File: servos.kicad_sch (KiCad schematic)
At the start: 16 parts, among them J10 Conn_01x03_Male, J18 Conn_01x03_Male, J19 Conn_01x03_Male, J5 Conn_01x03_Male, J6 Conn_01x03_Male, J7 Conn_01x03_Male, J8 Conn_01x03_Male, J9 Conn_01x03_Male, Q6 DMN2011UTS

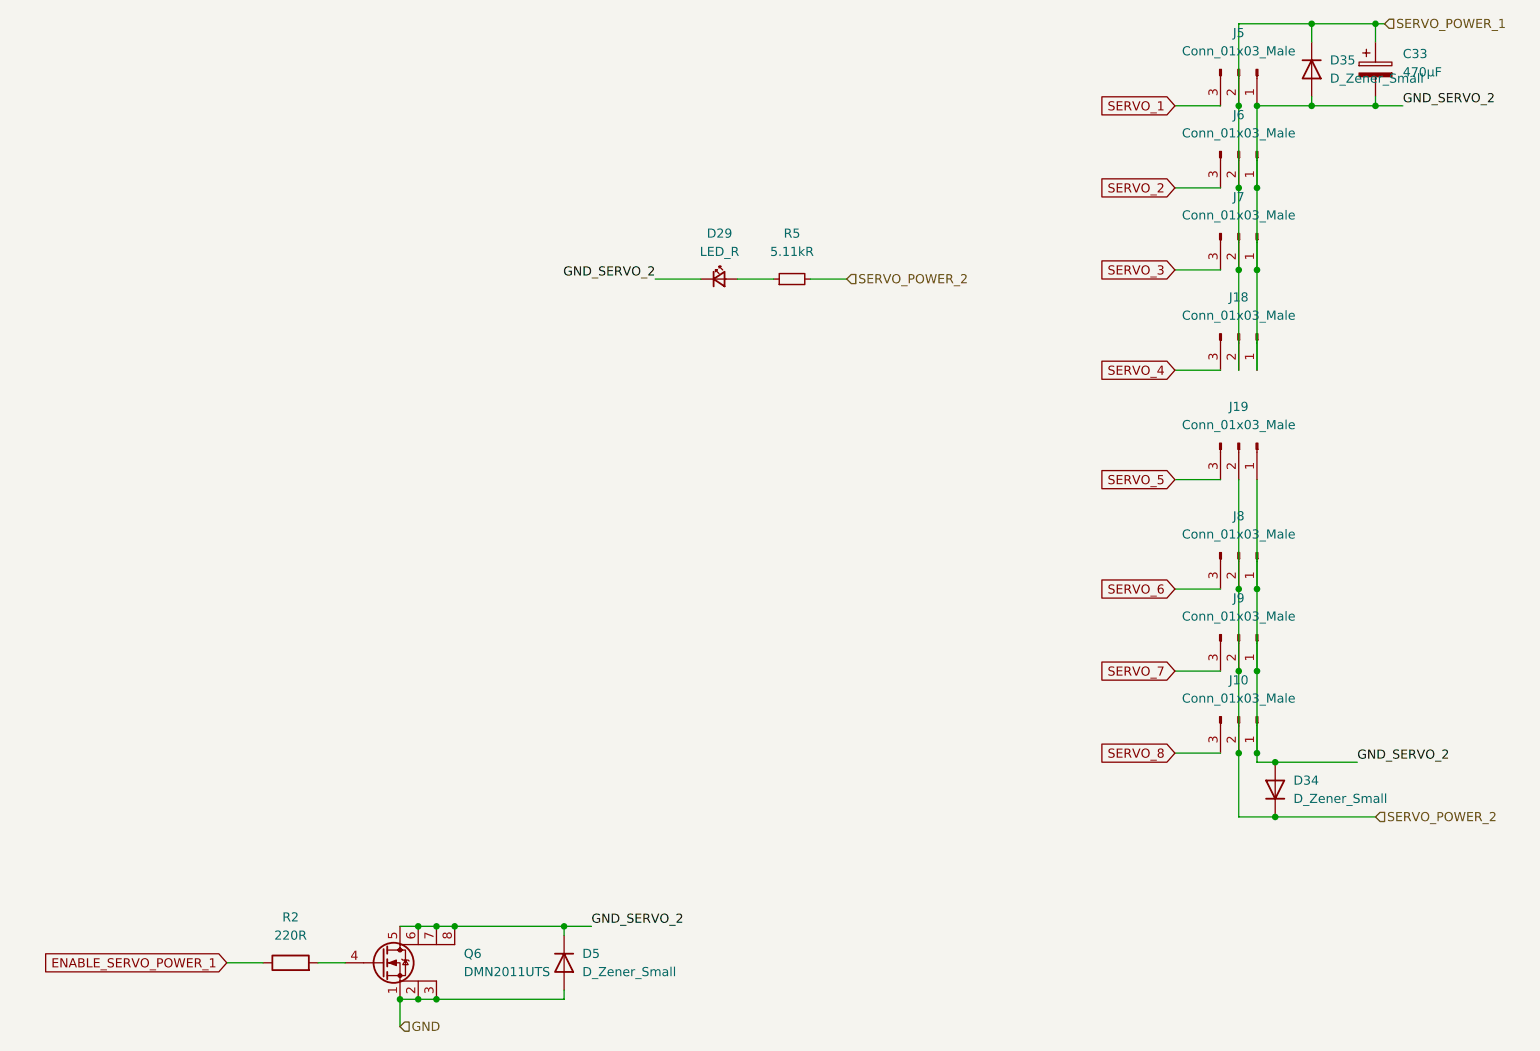
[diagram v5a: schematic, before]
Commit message: update BOM + add big capas (do not take DNP into account)
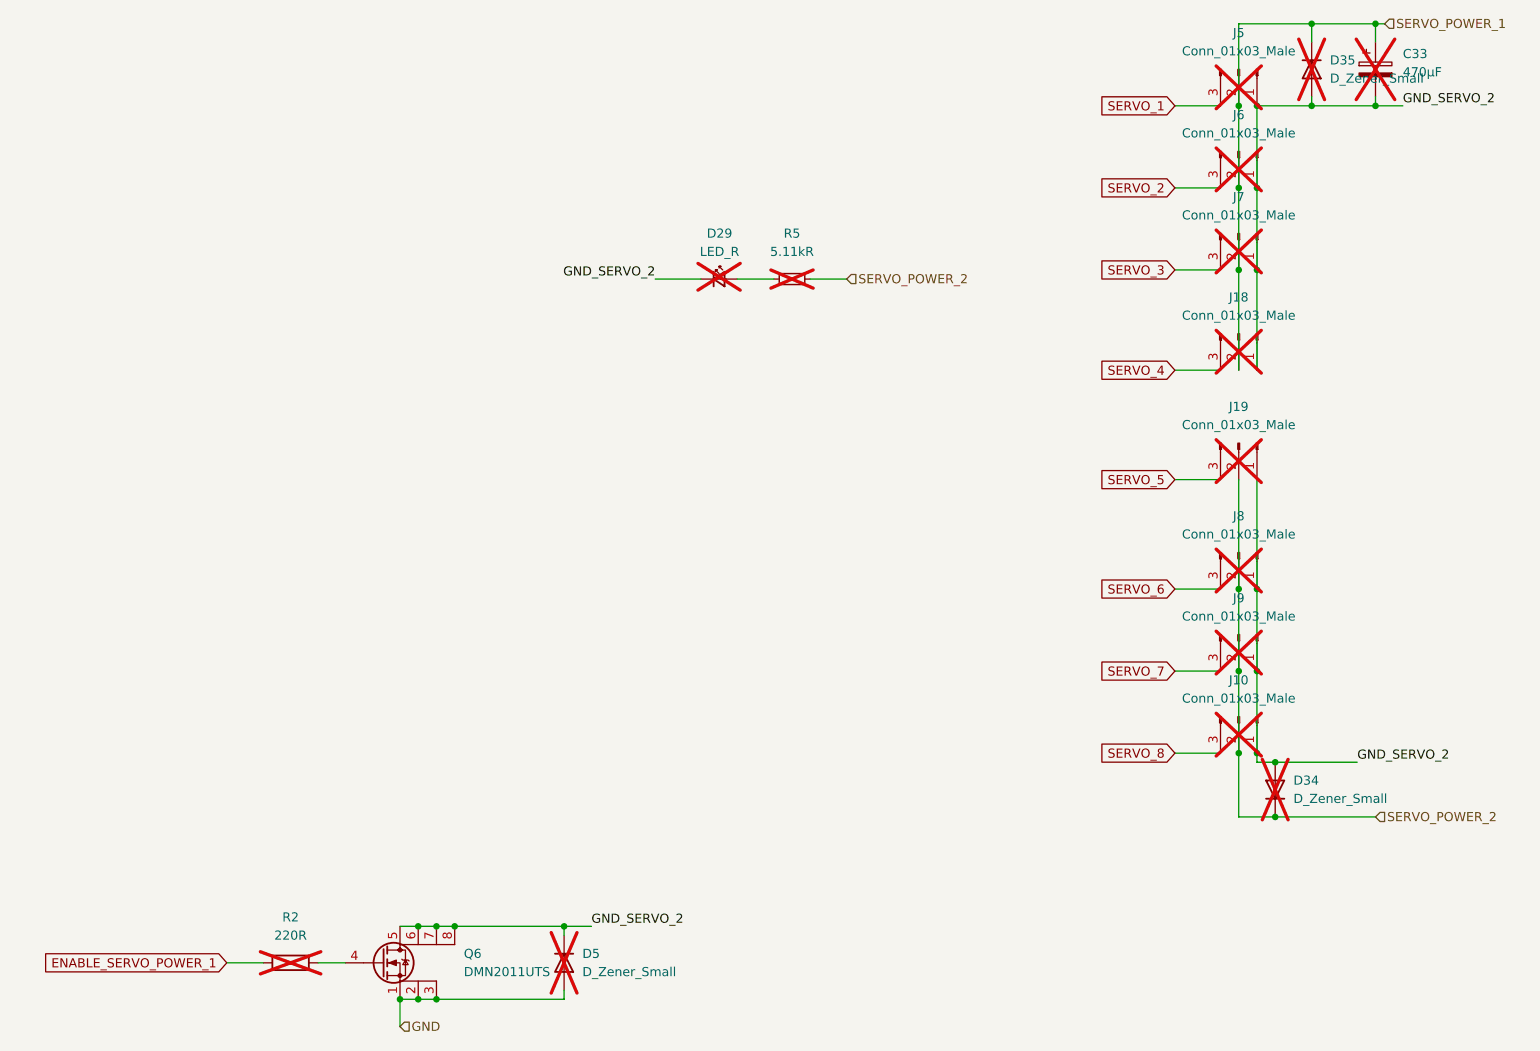
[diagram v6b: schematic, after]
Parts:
- C33, D29, D34, D35, D5, J10, J18, J19, J5, J6, J7, J8, J9, R2, R5: now not fitted
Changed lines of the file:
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@@
 		(in_bom yes)
 		(on_board yes)
-		(dnp no)
+		(dnp yes)
 		(fields_autoplaced yes)
 		(property "Reference" "D5"
@@
 		(in_bom yes)
 		(on_board yes)
-		(dnp no)
+		(dnp yes)
 		(fields_autoplaced yes)
 		(property "Reference" "J7"
@@
 		(in_bom yes)
 		(on_board yes)
-		(dnp no)
+		(dnp yes)
 		(property "Reference" "J19"
 			(at 210.82 99.06 90)
@@
 		(in_bom yes)
 		(on_board yes)
-		(dnp no)
+		(dnp yes)
 		(fields_autoplaced yes)
 		(property "Reference" "D29"
@@
 		(in_bom yes)
 		(on_board yes)
-		(dnp no)
+		(dnp yes)
 		(fields_autoplaced yes)
 		(property "Reference" "J5"
@@
 		(in_bom yes)
 		(on_board yes)
-		(dnp no)
+		(dnp yes)
 		(fields_autoplaced yes)
 		(property "Reference" "C33"
@@
 		(in_bom yes)
 		(on_board yes)
-		(dnp no)
+		(dnp yes)
 		(fields_autoplaced yes)
 		(property "Reference" "D34"
@@
 		(in_bom yes)
 		(on_board yes)
-		(dnp no)
+		(dnp yes)
 		(fields_autoplaced yes)
 		(property "Reference" "J6"
@@
 		(in_bom yes)
 		(on_board yes)
-		(dnp no)
+		(dnp yes)
 		(fields_autoplaced yes)
 		(property "Reference" "D35"
@@
 		(in_bom yes)
 		(on_board yes)
-		(dnp no)
+		(dnp yes)
 		(fields_autoplaced yes)
 		(property "Reference" "R5"
@@
 		(in_bom yes)
 		(on_board yes)
-		(dnp no)
+		(dnp yes)
 		(fields_autoplaced yes)
 		(property "Reference" "J10"
@@
 		(in_bom yes)
 		(on_board yes)
-		(dnp no)
+		(dnp yes)
 		(fields_autoplaced yes)
 		(property "Reference" "J18"
@@
 		(in_bom yes)
 		(on_board yes)
-		(dnp no)
+		(dnp yes)
 		(fields_autoplaced yes)
 		(property "Reference" "J9"
@@
 		(in_bom yes)
 		(on_board yes)
-		(dnp no)
+		(dnp yes)
 		(property "Reference" "J8"
 			(at 210.82 114.3 90)
@@
 		(in_bom yes)
 		(on_board yes)
-		(dnp no)
+		(dnp yes)
 		(fields_autoplaced yes)
 		(property "Reference" "R2"

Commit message: fix DNP (was just for checking what was to be bought)
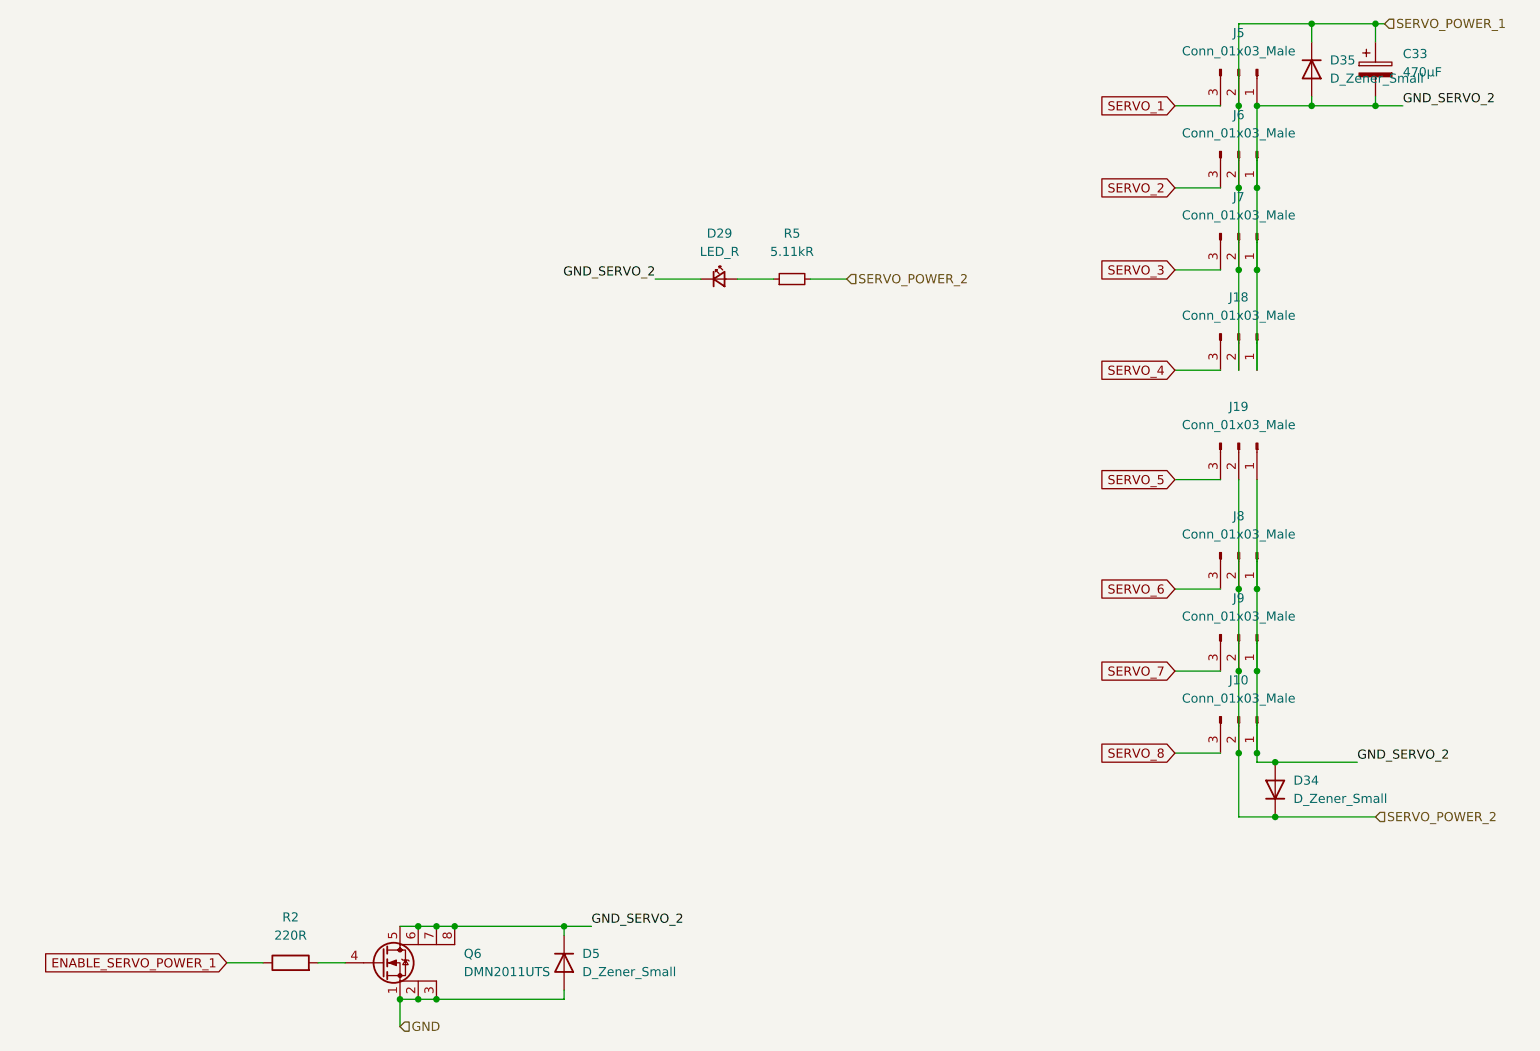
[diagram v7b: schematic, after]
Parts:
- C33, D29, D34, D35, D5, J10, J18, J19, J5, J6, J7, J8, J9, R2, R5: now fitted
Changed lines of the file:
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@@
 		(in_bom yes)
 		(on_board yes)
-		(dnp yes)
+		(dnp no)
 		(fields_autoplaced yes)
 		(property "Reference" "D5"
@@
 		(in_bom yes)
 		(on_board yes)
-		(dnp yes)
+		(dnp no)
 		(fields_autoplaced yes)
 		(property "Reference" "J7"
@@
 		(in_bom yes)
 		(on_board yes)
-		(dnp yes)
+		(dnp no)
 		(property "Reference" "J19"
 			(at 210.82 99.06 90)
@@
 		(in_bom yes)
 		(on_board yes)
-		(dnp yes)
+		(dnp no)
 		(fields_autoplaced yes)
 		(property "Reference" "D29"
@@
 		(in_bom yes)
 		(on_board yes)
-		(dnp yes)
+		(dnp no)
 		(fields_autoplaced yes)
 		(property "Reference" "J5"
@@
 		(in_bom yes)
 		(on_board yes)
-		(dnp yes)
+		(dnp no)
 		(fields_autoplaced yes)
 		(property "Reference" "C33"
@@
 		(in_bom yes)
 		(on_board yes)
-		(dnp yes)
+		(dnp no)
 		(fields_autoplaced yes)
 		(property "Reference" "D34"
@@
 		(in_bom yes)
 		(on_board yes)
-		(dnp yes)
+		(dnp no)
 		(fields_autoplaced yes)
 		(property "Reference" "J6"
@@
 		(in_bom yes)
 		(on_board yes)
-		(dnp yes)
+		(dnp no)
 		(fields_autoplaced yes)
 		(property "Reference" "D35"
@@
 		(in_bom yes)
 		(on_board yes)
-		(dnp yes)
+		(dnp no)
 		(fields_autoplaced yes)
 		(property "Reference" "R5"
@@
 		(in_bom yes)
 		(on_board yes)
-		(dnp yes)
+		(dnp no)
 		(fields_autoplaced yes)
 		(property "Reference" "J10"
@@
 		(in_bom yes)
 		(on_board yes)
-		(dnp yes)
+		(dnp no)
 		(fields_autoplaced yes)
 		(property "Reference" "J18"
@@
 		(in_bom yes)
 		(on_board yes)
-		(dnp yes)
+		(dnp no)
 		(fields_autoplaced yes)
 		(property "Reference" "J9"
@@
 		(in_bom yes)
 		(on_board yes)
-		(dnp yes)
+		(dnp no)
 		(property "Reference" "J8"
 			(at 210.82 114.3 90)
@@
 		(in_bom yes)
 		(on_board yes)
-		(dnp yes)
+		(dnp no)
 		(fields_autoplaced yes)
 		(property "Reference" "R2"
